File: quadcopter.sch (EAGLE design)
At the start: 61 parts, among them J1 ISP, J4 SIP-10_TH-254X10, M1 MOTOR_PADS, M2 MOTOR_PADS, M3 MOTOR_PADS, M4 MOTOR_PADS, U1 ATMEGA128RFA1, Y1 16MHz

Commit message: Schematic edited on April 24th
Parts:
- added J2: (no value), quadparts:MALE_HEADER_2POS-2X1-0.1IN
- added LED1, LED4: BLUE, LEDs:LTST-C193TBKT-5ADISCRETE_LED
- added R12, R13: 10, quadparts_prebuilt:RESISTOR_SMD-2012-0805-10
- added R14, R15: 5.1K, quadparts_prebuilt:RESISTOR_SMD-2012-0805-5.1K
- LED2, LED3: device LEDs:LTST-C193TBKT-5ADISCRETE_LED -> Yueqi Wang-Lab2:LED5MM
- R10, R11: value 10 -> 330; device quadparts_prebuilt:RESISTOR_SMD-2012-0805-10 -> quadparts_prebuilt:RESISTOR_SMD-2012-0805-330
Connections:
- removed net FILTERED: MOFSET1.G, MOFSET2.G, MOFSET3.G, MOFSET4.G, R1.2, R2.2, R3.2, R4.2, R5.2, R6.2, R7.2, R8.2
- removed net FLYBACK: D1.A, D2.A, D3.A, D4.A, M1.V-, M2.V-, M3.V-, M4.V-, MOFSET1.D, MOFSET2.D, MOFSET3.D, MOFSET4.D
- removed net N$20: JP2.2, U1.PD2(RXD1/INT2)
- removed net N$21: JP2.3, U1.PD3(TXD1/INT3)
- new net FILTERED_1: MOFSET1.G, R3.2, R4.2
- new net FILTERED_2: MOFSET2.G, R1.2, R2.2
- new net FILTERED_3: MOFSET3.G, R5.2, R6.2
- new net FILTERED_4: MOFSET4.G, R7.2, R8.2
- new net FLYBACK_1: D2.A, M2.V-, MOFSET1.D
- new net FLYBACK_2: D1.A, M1.V-, MOFSET2.D
- new net FLYBACK_3: D3.A, M3.V-, MOFSET3.D
- new net FLYBACK_4: D4.A, M4.V-, MOFSET4.D
- new net N$24: C15.2
- new net N$3: LED4.A, R12.1
- new net N$4: JP2.2, U1.PD3(TXD1/INT3)
- new net N$5: JP2.3, U1.PD2(RXD1/INT2)
- new net N$6: LED1.A, R13.1
- new net N$7: BATT1.P, J2.1
- net BAT_GND: now also C1.-, C3.-, C5.-, C7.-
- net GND: now also LED1.C, LED4.C; no longer C1.-, C15.2, C3.-, C5.-, C7.-, IMU1.SDO_M
- net PE3: now also C6.1, R7.1; no longer C4.1, R5.1
- net PE4: now also C4.1, R5.1; no longer C6.1, R7.1
- net PG0: now also R12.2
- net PG1: now also R13.2
- net SCL: now also R14.1
- net SDA: now also R15.1
- net VBAT: now also J2.2; no longer BATT1.P
- net VCC: now also IMU1.SDO_M, R14.2, R15.2
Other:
- moved on the sheet: A1, B1, BATT1, C1, C10, C11, C12, C13, C14, C15, C16, C17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

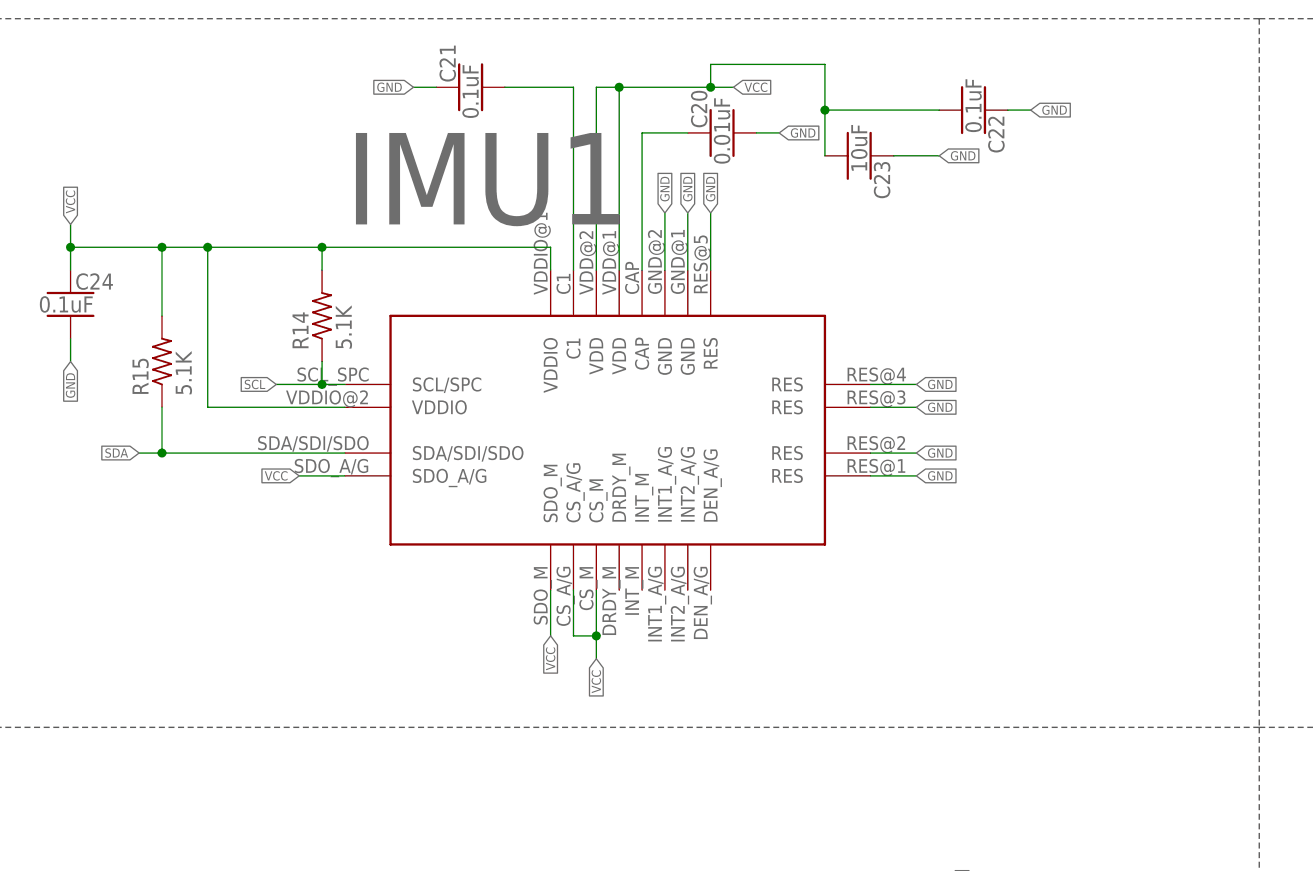
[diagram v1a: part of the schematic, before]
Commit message: Edited IMU and MOSFET pad size
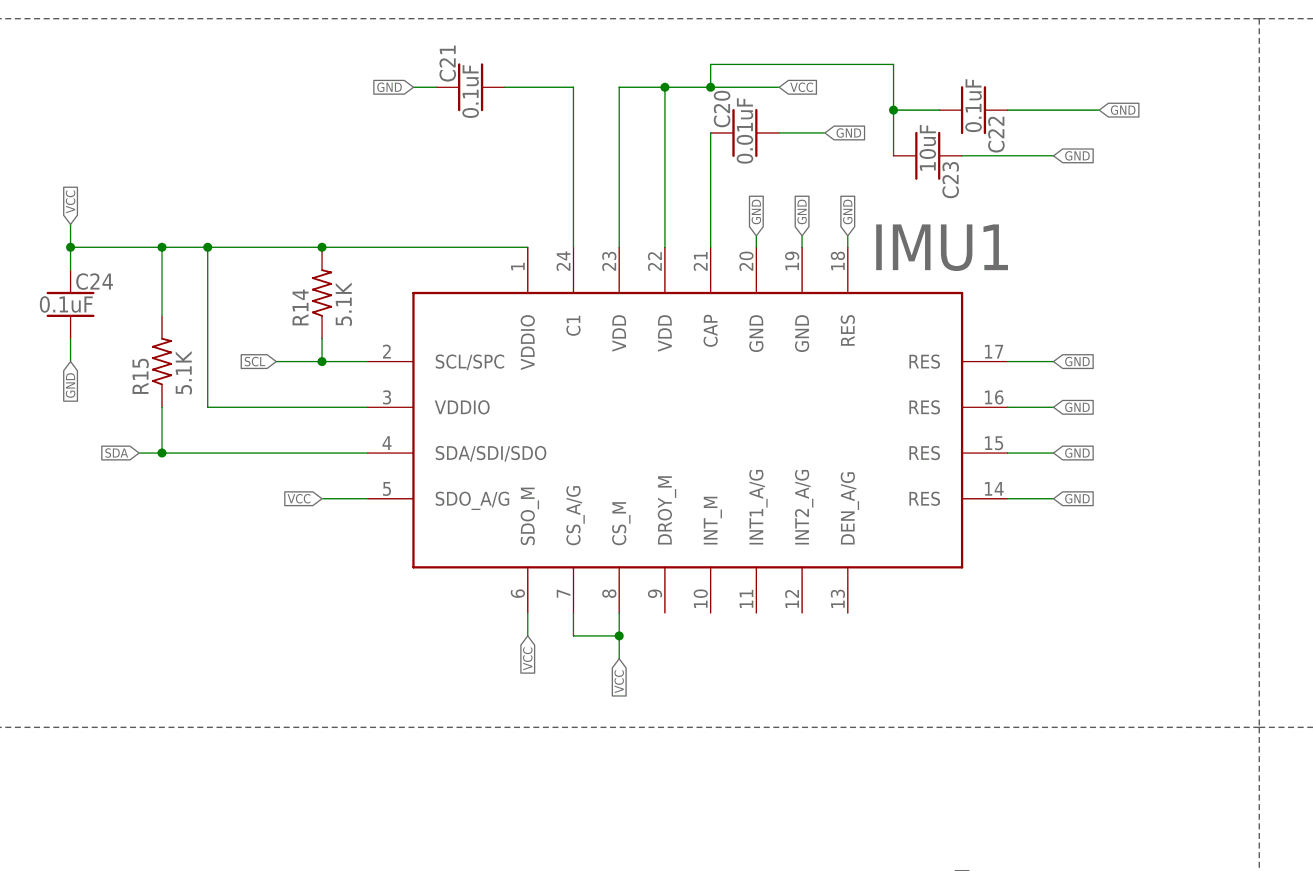
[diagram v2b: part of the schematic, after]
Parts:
- IMU1: value LSM9DS1_9AXIS_IMUIMU -> 9_AXIS_IMU; device quadparts:LSM9DS1_9AXIS_IMUIMU -> quadparts_yupei:9_AXIS_IMU
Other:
- moved on the sheet: C20, C23, IMU1, R14

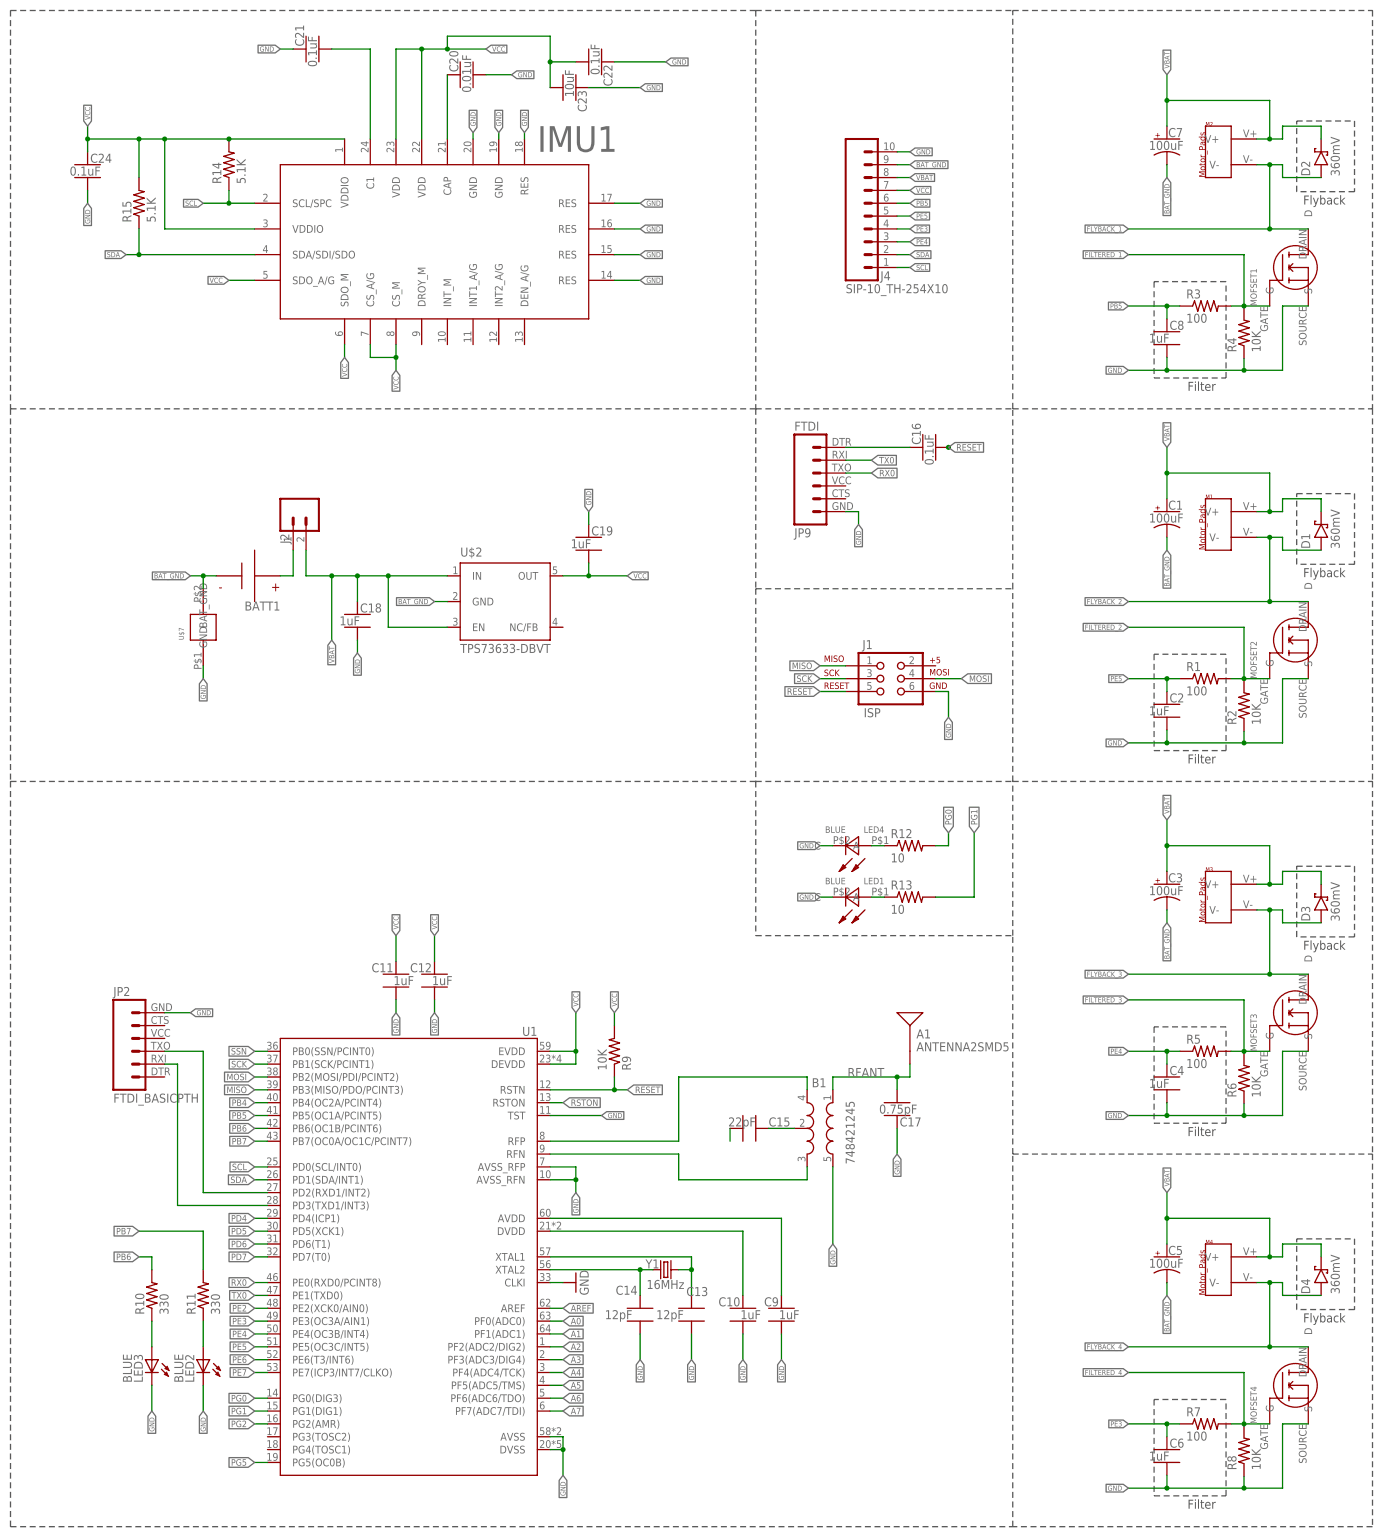
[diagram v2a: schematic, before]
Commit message: Modified schematic and initial board
Schematic has been modified based on design review and board has been layout.
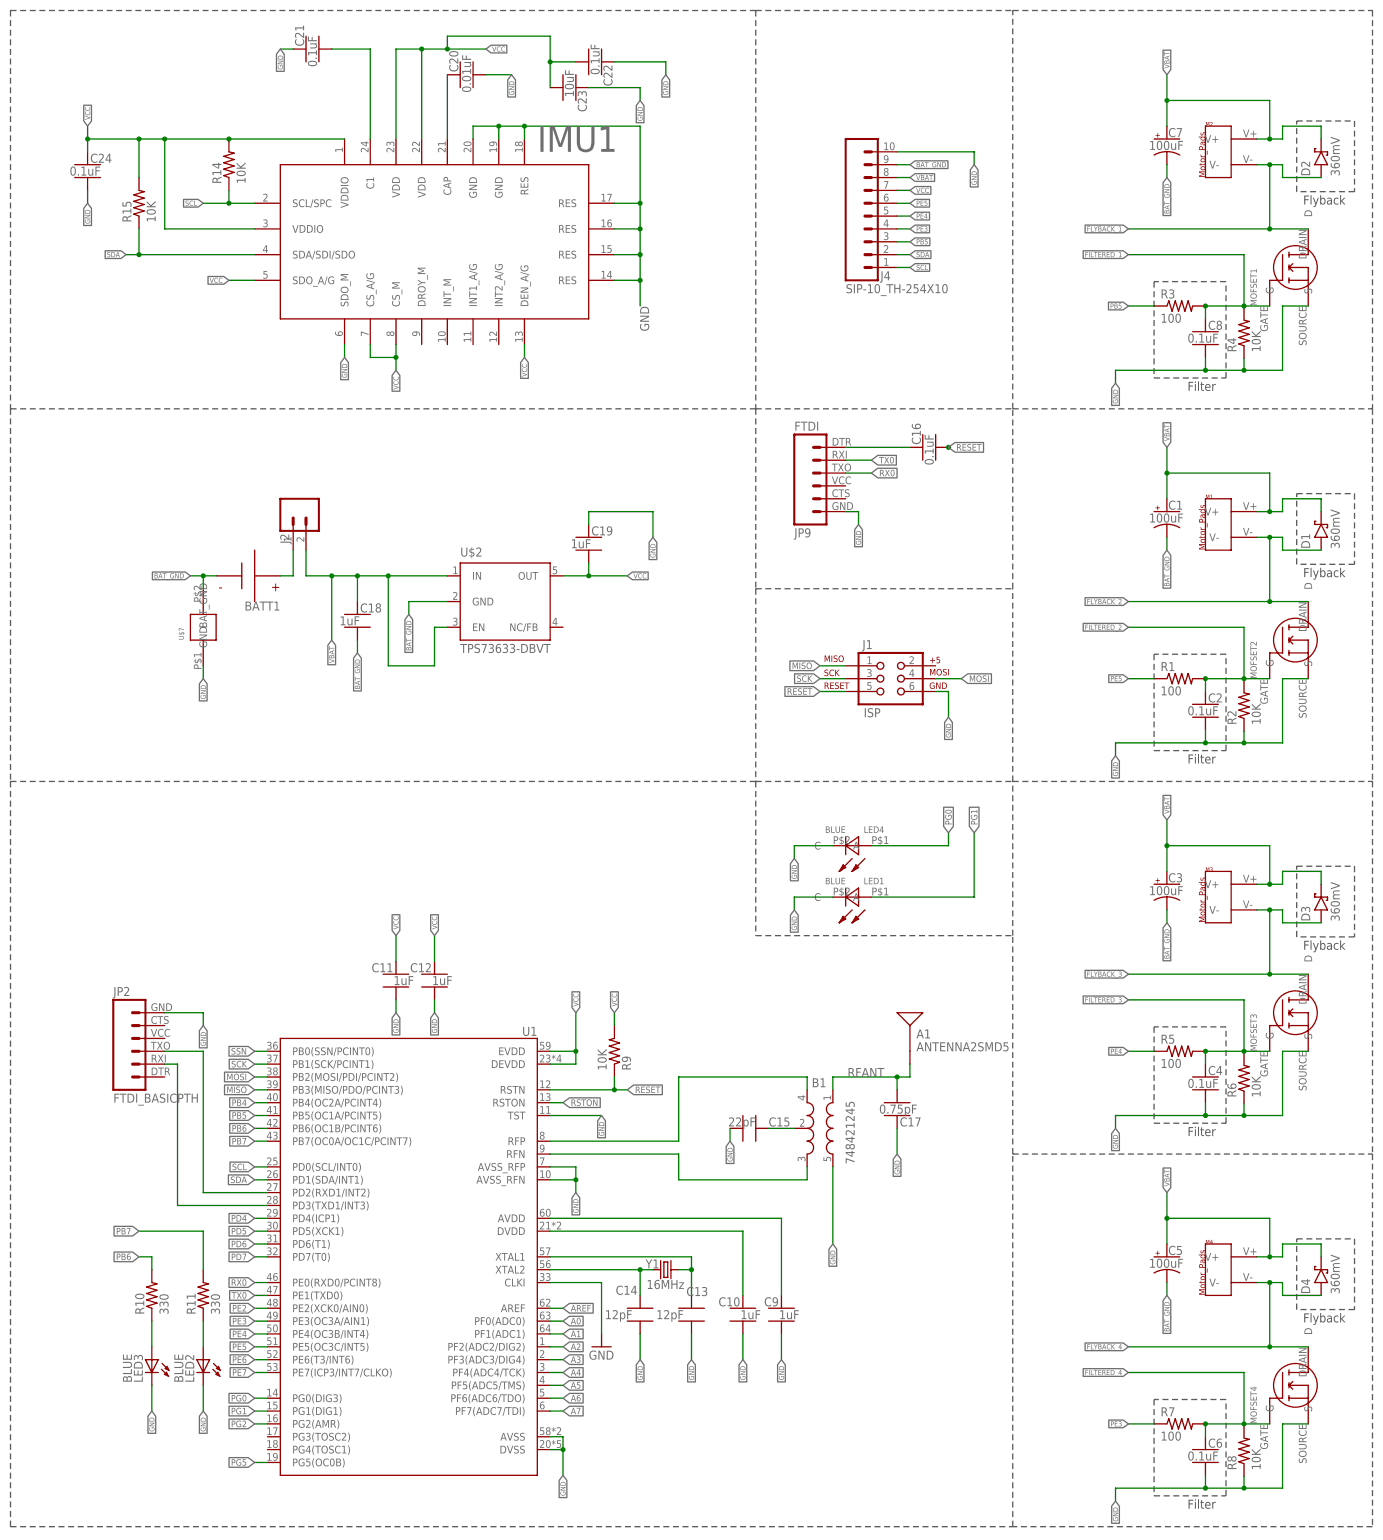
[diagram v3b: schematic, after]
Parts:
- removed R12, R13: 10, quadparts_prebuilt:RESISTOR_SMD-2012-0805-10
- C2, C4, C6, C8: value 1uF -> 0.1uF; device quadparts_prebuilt:CAPACITOR-NP_SMD-2012-0805_CERAMIC-1UF -> quadparts_prebuilt:CAPACITOR-NP_SMD-2012-0805_CERAMIC-0.1UF
- R14, R15: value 5.1K -> 10K; device quadparts_prebuilt:RESISTOR_SMD-2012-0805-5.1K -> quadparts_prebuilt:RESISTOR_SMD-2012-0805-10K
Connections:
- removed net N$24: C15.2
- removed net N$3: LED4.A, R12.1
- removed net N$6: LED1.A, R13.1
- net BAT_GND: now also C18.2
- net FILTERED_1: now also C8.1
- net FILTERED_2: now also C2.1
- net FILTERED_3: now also C4.1
- net FILTERED_4: now also C6.1
- net GND: now also C15.2, IMU1.SDO_M; no longer C18.2
- net PB5: now also J4.3; no longer C8.1, J4.6
- net PE3: no longer C6.1
- net PE4: now also J4.5; no longer C4.1, J4.3
- net PE5: now also J4.6; no longer C2.1, J4.5
- net PG0: now also LED4.A; no longer R12.2
- net PG1: now also LED1.A; no longer R13.2
- net VCC: now also IMU1.DEN_A/G; no longer IMU1.SDO_M
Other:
- moved on the sheet: C2, C4, C6, C8, R1, R3, R5, R7

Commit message: Version before generating cam
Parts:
- LED2, LED3: value BLUE -> green; device Yueqi Wang-Lab2:LED5MM -> quadparts_prebuilt:DIODE-LED_SMD-2012-0805-GREEN
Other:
- moved on the sheet: LED2, LED3
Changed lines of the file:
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@@
 <part name="JP9" library="quadparts_prebuilt" deviceset="FTDI_BASIC" device="PTH" value="FTDI"/>
 <part name="C16" library="quadparts_prebuilt" deviceset="CAPACITOR-NP_" device="SMD-2012-0805_CERAMIC-0.1UF" value="0.1uF"/>
-<part name="LED2" library="Yueqi Wang-Lab2" deviceset="LED" device="5MM" value="BLUE"/>
+<part name="LED2" library="quadparts_prebuilt" deviceset="DIODE-LED_" device="SMD-2012-0805-GREEN" value="green"/>
 <part name="C17" library="quadparts_prebuilt" deviceset="CAPACITOR-NP_" device="SMD-2012-0805_CERAMIC-0.75PF" value="0.75pF"/>
-<part name="LED3" library="Yueqi Wang-Lab2" deviceset="LED" device="5MM" value="BLUE"/>
+<part name="LED3" library="quadparts_prebuilt" deviceset="DIODE-LED_" device="SMD-2012-0805-GREEN" value="green"/>
 <part name="R10" library="quadparts_prebuilt" deviceset="RESISTOR_" device="SMD-2012-0805-330" value="330"/>
 <part name="R11" library="quadparts_prebuilt" deviceset="RESISTOR_" device="SMD-2012-0805-330" value="330"/>
@@
 <instance part="JP9" gate="G$1" x="38.1" y="45.72" rot="MR180"/>
 <instance part="C16" gate="G$1" x="58.42" y="50.8" rot="R90"/>
-<instance part="LED2" gate="G$1" x="-83.82" y="-129.54" rot="MR0"/>
+<instance part="LED2" gate="G$1" x="-83.82" y="-129.54" rot="MR270"/>
 <instance part="C17" gate="G$1" x="53.34" y="-81.28" rot="MR180"/>
-<instance part="LED3" gate="G$1" x="-93.98" y="-129.54" rot="MR0"/>
+<instance part="LED3" gate="G$1" x="-93.98" y="-129.54" rot="MR270"/>
 <instance part="R10" gate="G$1" x="-93.98" y="-116.84" rot="R90"/>
 <instance part="R11" gate="G$1" x="-83.82" y="-116.84" rot="R90"/>

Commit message: New schematic after Prof. review on May 10th
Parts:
- added SW1: PUSHBUTTON_SMD-VERTICAL-1, quadparts_prebuilt:PUSHBUTTON_SMD-VERTICAL-1
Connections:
- net GND: now also SW1.2
- net RESET: now also SW1.1
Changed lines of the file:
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@@
 <part name="R14" library="quadparts_prebuilt" deviceset="RESISTOR_" device="SMD-2012-0805-10K" value="10K"/>
 <part name="R15" library="quadparts_prebuilt" deviceset="RESISTOR_" device="SMD-2012-0805-10K" value="10K"/>
+<part name="SW1" library="quadparts_prebuilt" deviceset="PUSHBUTTON_" device="SMD-VERTICAL-1"/>
 </parts>
 <sheets>
@@
 <instance part="R14" gate="G$1" x="-78.74" y="106.68" rot="R90"/>
 <instance part="R15" gate="G$1" x="-96.52" y="99.06" rot="R90"/>
+<instance part="SW1" gate="G$1" x="12.7" y="-55.88" rot="R270"/>
 </instances>
 <busses>
 </busses>
 <nets>
-<net name="GND" class="2">
+<net name="GND" class="0">
 <segment>
 <pinref part="U1" gate="G$1" pin="CLKI"/>
@@
 <label x="20.32" y="-86.36" size="1.016" layer="95" rot="R270" xref="yes"/>
 </segment>
+<segment>
+<pinref part="SW1" gate="G$1" pin="2"/>
+<wire x1="10.16" y1="-60.96" x2="10.16" y2="-63.5" width="0.1524" layer="91"/>
+<label x="10.16" y="-63.5" size="1.016" layer="95" rot="R270" xref="yes"/>
+</segment>
 </net>
 <net name="FILTERED_1" class="2">
@@
 <wire x1="-15.24" y1="-76.2" x2="-2.54" y2="-76.2" width="0.1524" layer="91"/>
 <wire x1="-2.54" y1="-76.2" x2="-2.54" y2="-73.66" width="0.1524" layer="91"/>
-<wire x1="-2.54" y1="-76.2" x2="0" y2="-76.2" width="0.1524" layer="91"/>
 <junction x="-2.54" y="-76.2"/>
-<label x="0" y="-76.2" size="1.27" layer="95" rot="MR180" xref="yes"/>
+<label x="22.86" y="-50.8" size="1.27" layer="95" rot="MR180" xref="yes"/>
+<wire x1="-2.54" y1="-76.2" x2="2.54" y2="-76.2" width="0.1524" layer="91"/>
+<wire x1="2.54" y1="-76.2" x2="2.54" y2="-50.8" width="0.1524" layer="91"/>
+<wire x1="2.54" y1="-50.8" x2="10.16" y2="-50.8" width="0.1524" layer="91"/>
+<pinref part="SW1" gate="G$1" pin="1"/>
+<wire x1="10.16" y1="-50.8" x2="22.86" y2="-50.8" width="0.1524" layer="91"/>
+<junction x="10.16" y="-50.8"/>
 </segment>
 <segment>
@@
 </segment>
 </net>
-<net name="PE5" class="2">
+<net name="PE5" class="0">
 <segment>
 <pinref part="U1" gate="G$1" pin="PE5(OC3C/INT5)"/>
@@
 </segment>
 </net>
-<net name="PE4" class="2">
+<net name="PE4" class="0">
 <segment>
 <pinref part="U1" gate="G$1" pin="PE4(OC3B/INT4)"/>
@@
 </segment>
 </net>
-<net name="PE3" class="2">
+<net name="PE3" class="0">
 <segment>
 <pinref part="U1" gate="G$1" pin="PE3(OC3A/AIN1)"/>
@@
 </segment>
 </net>
-<net name="PB5" class="2">
+<net name="PB5" class="0">
 <segment>
 <pinref part="U1" gate="G$1" pin="PB5(OC1A/PCINT5)"/>
@@
 </segment>
 </net>
-<net name="N$7" class="0">
+<net name="N$7" class="2">
 <segment>
 <pinref part="BATT1" gate="G$1" pin="P"/>
